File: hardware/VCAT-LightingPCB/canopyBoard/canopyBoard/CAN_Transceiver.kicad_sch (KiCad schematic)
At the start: 9 parts, among them IC2 TCAN3413DR

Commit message: added current check, please dont overwrite my file again
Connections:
- net 3.3v renamed 3.3V
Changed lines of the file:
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@@
 		)
 	)
-	(hierarchical_label "3.3v"
+	(hierarchical_label "3.3V"
 		(shape input)
 		(at 149.86 67.31 0)
@@
 		)
 	)
-	(hierarchical_label "3.3v"
+	(hierarchical_label "3.3V"
 		(shape input)
 		(at 87.63 63.5 0)

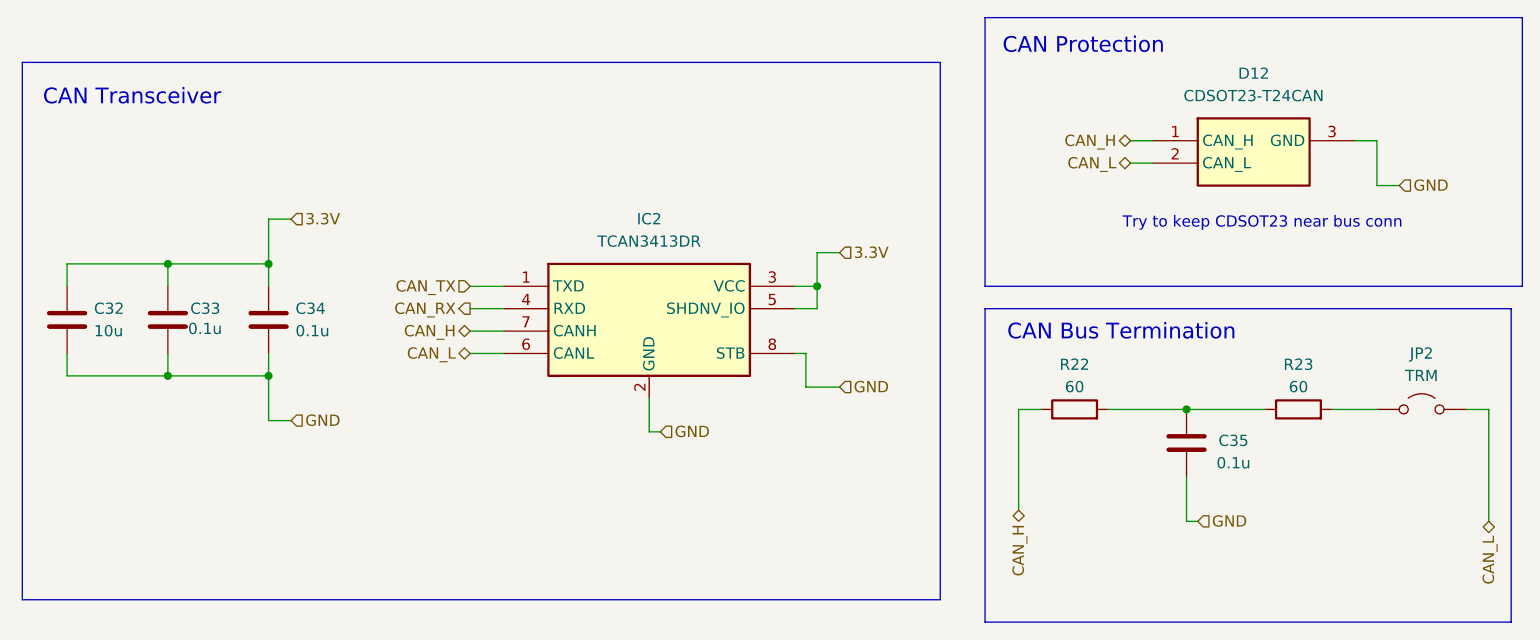
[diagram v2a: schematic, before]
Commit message: Untrack KiCad .history, convert KiCAD-Sharepoint to a submodule, remove LightsPCB
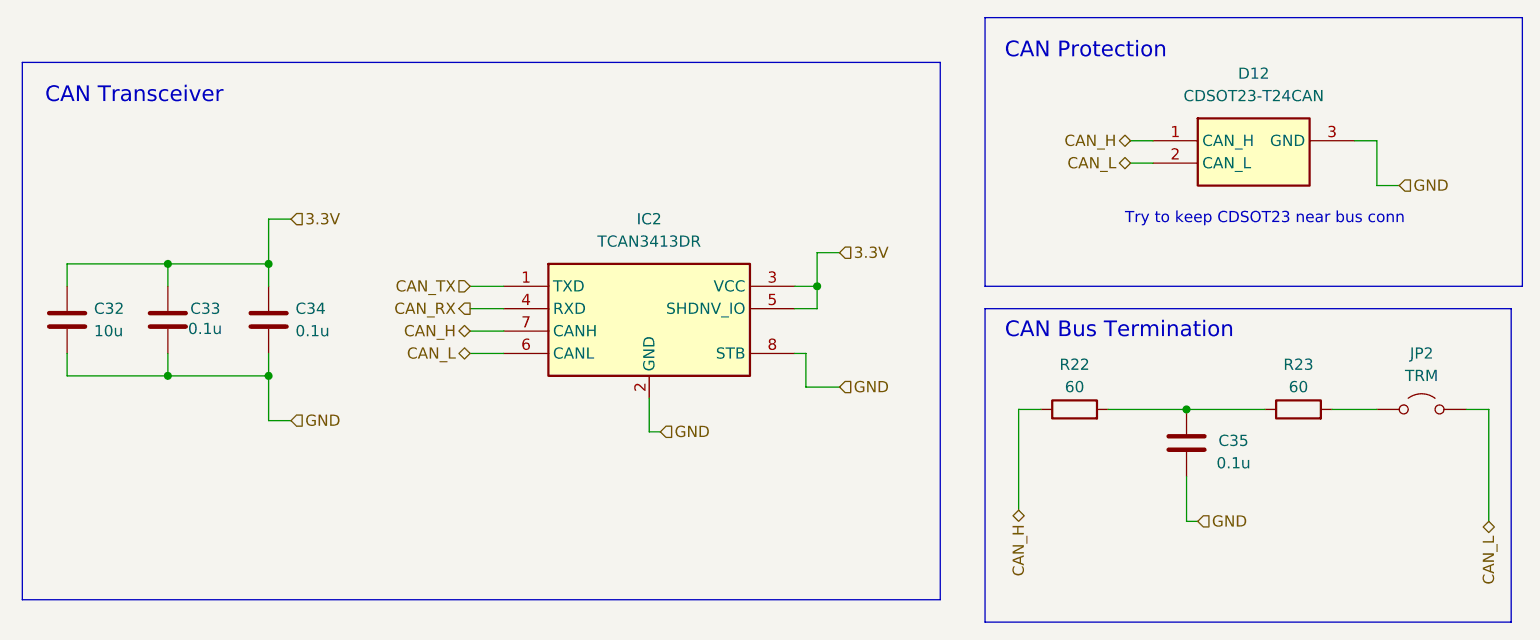
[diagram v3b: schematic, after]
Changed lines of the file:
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@@
 	(text "CAN Transceiver\n"
 		(exclude_from_sim no)
-		(at 69.596 49.784 0)
+		(at 69.85 49.53 0)
 		(effects
 			(font
@@
 	(text "Try to keep CDSOT23 near bus conn"
 		(exclude_from_sim no)
-		(at 197.866 64.008 0)
+		(at 198.12 63.5 0)
 		(effects
 			(font
@@
 	(text "CAN Protection"
 		(exclude_from_sim no)
-		(at 177.546 43.942 0)
+		(at 177.8 44.45 0)
 		(effects
 			(font
@@
 	(text "CAN Bus Termination\n"
 		(exclude_from_sim no)
-		(at 181.864 76.454 0)
+		(at 181.61 76.2 0)
 		(effects
 			(font
